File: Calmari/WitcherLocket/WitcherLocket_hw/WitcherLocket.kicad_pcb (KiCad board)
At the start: 2 copper layers, 41 x 50 mm, 31 parts, among them SW1 SWITCH_2X, SW2 SWITCH_2X, SW3 SWITCH_2X, SW4 SWITCH_2X

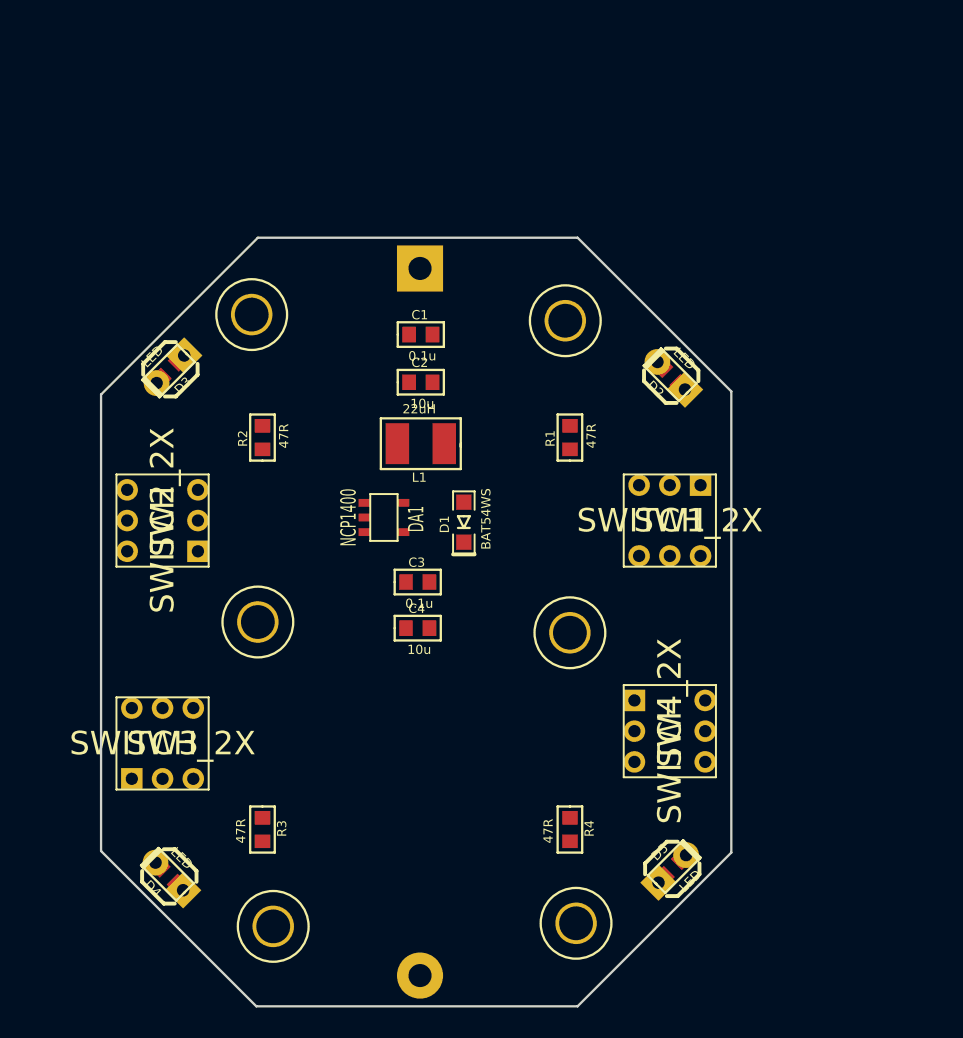
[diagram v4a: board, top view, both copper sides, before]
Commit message: 
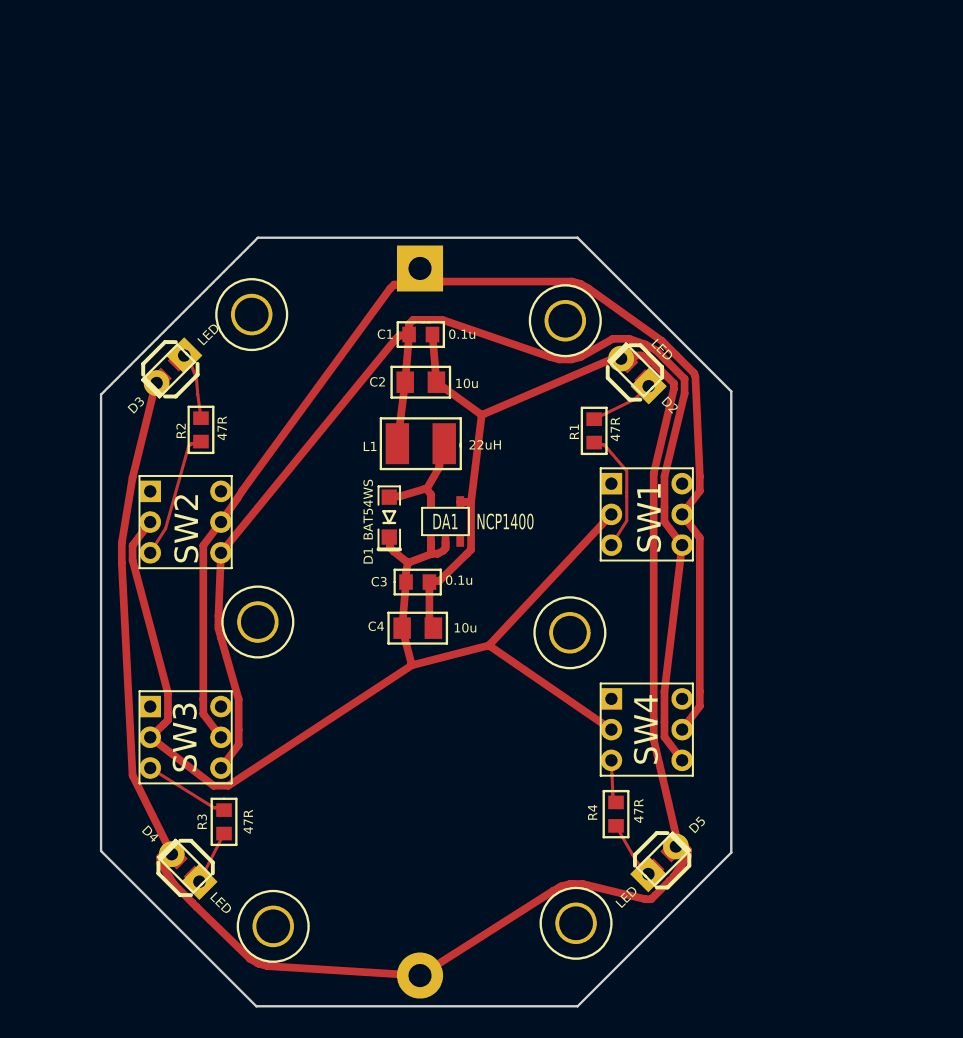
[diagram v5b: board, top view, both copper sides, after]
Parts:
- C2, C4: footprint CAP_0603 -> CAP_0805
- moved D1 4.86 mm to (153.2, 117.2)
- moved R2 4.03 mm to (141.0, 111.5)
- moved DA1 4.02 mm to (156.9, 117.5), turned to 0 degrees
- moved R4 3.16 mm to (168.0, 136.5)
- moved R3 2.55 mm to (142.5, 137.0)
- moved D6 2.37 mm to (169.2, 107.8)
- moved D2 2.30 mm to (169.3, 107.7)
- moved R1 1.64 mm to (166.6, 111.6)
- moved SW1 1.55 mm to (170.0, 117.0), turned to 270 degrees
- moved SW3 1.55 mm to (140.0, 131.5), turned to 270 degrees
- moved SW2 1.50 mm to (140.0, 117.5), turned to 270 degrees
- moved SW4 1.50 mm to (170.0, 131.0)
- moved D4 1.23 mm to (140.0, 140.0)
- moved D8 1.19 mm to (140.0, 140.0)
- moved D9 0.87 mm to (171.0, 139.5)
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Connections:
- SW1 pad 4: (no net) -> /PWR_IN
- SW1 pad 6: /PWR_IN -> (no net)
- SW2 pad 4: (no net) -> /PWR_IN
- SW2 pad 6: /PWR_IN -> (no net)
- SW3 pad 4: (no net) -> /PWR_IN
- SW3 pad 6: /PWR_IN -> (no net)
- SW4 pad 4: (no net) -> /PWR_IN
- SW4 pad 6: /PWR_IN -> (no net)
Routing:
- net GND: track 0.00 -> 143.4 mm
- net /PWR_IN: track 0.00 -> 86.9 mm
- net +BATT: track 0.00 -> 80.5 mm
- net +3.3V: track 0.00 -> 75.1 mm
- net N-000002: track 0.00 -> 8.32 mm
- net N-0000011: track 0.00 -> 8.03 mm
- net /Lout: track 0.00 -> 6.66 mm
- net N-000007: track 0.00 -> 5.57 mm
- net N-0000024: track 0.00 -> 5.11 mm
- net N-0000022: track 0.00 -> 4.69 mm
- net N-0000013: track 0.00 -> 4.31 mm
- net N-0000012: track 0.00 -> 4.04 mm
- net N-0000010: track 0.00 -> 2.80 mm
- added copper zone on F.Cu, net GND
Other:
- rule pad_to_mask_clearance: 0 -> 0.1

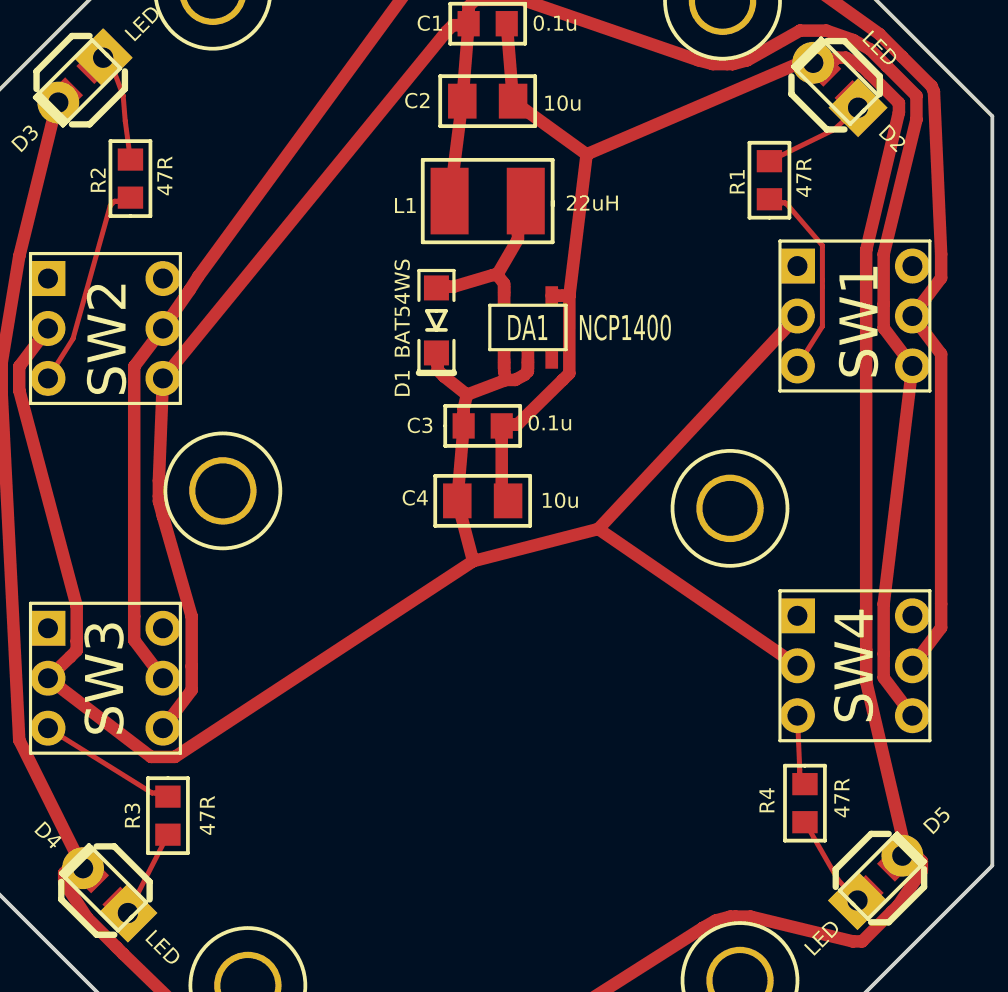
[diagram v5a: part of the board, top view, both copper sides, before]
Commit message: led resistors change
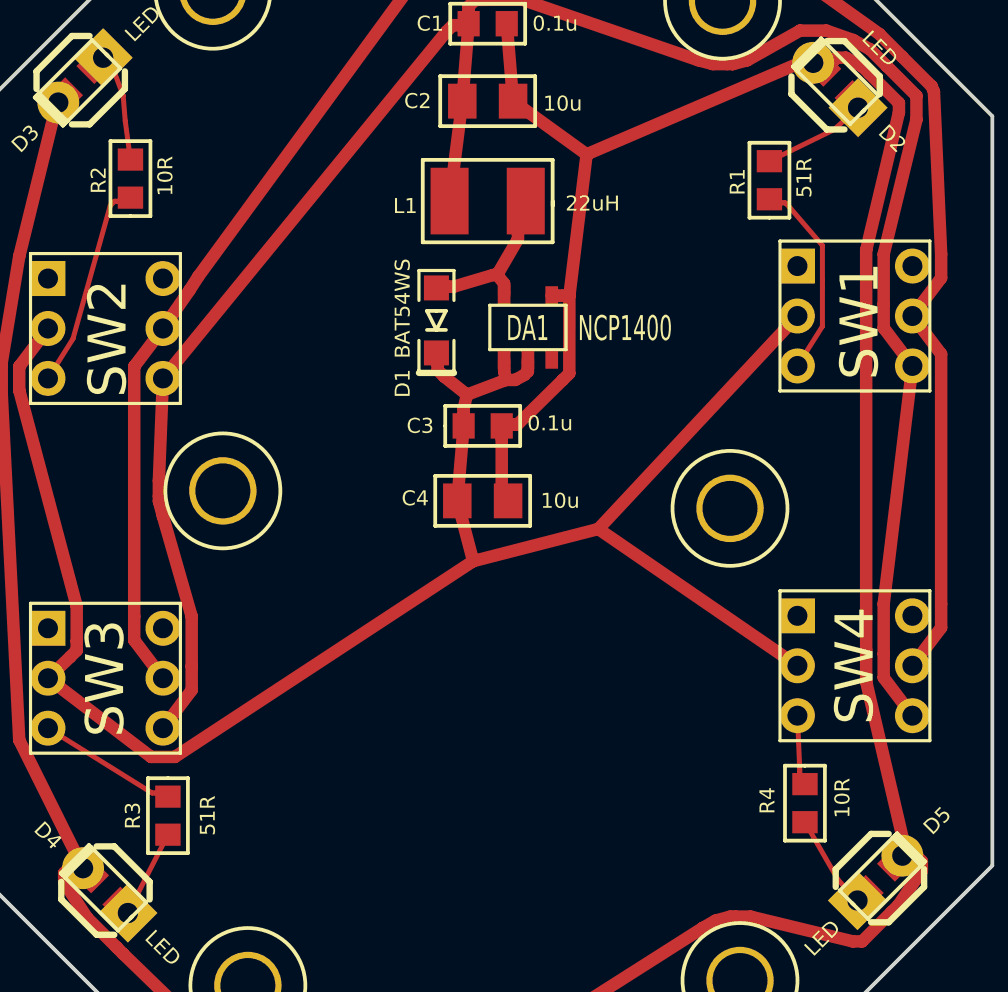
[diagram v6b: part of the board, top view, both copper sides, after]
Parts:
- R1, R3: value 47R -> 51R
- R2, R4: value 47R -> 10R
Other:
- board text added: "Blue"
- board text added: "Green"
- board text added: "Red"
- board text added: "Yellow"
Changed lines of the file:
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@@
-(kicad_pcb (version 3) (host pcbnew "(2013-03-19 BZR 4004)-stable")
+(kicad_pcb (version 3) (host pcbnew "(2013-05-16 BZR 4016)-stable")
   (general
     (links 45)
@@
     (area 133.4736 98.624863 175.9264 149.100001)
     (thickness 1.6)
-    (drawings 13)
+    (drawings 17)
     (tracks 238)
     (zones 0)
@@
       (usegerberextensions true)
       (excludeedgelayer true)
-      (linewidth 152400)
+      (linewidth 0.150000)
       (plotframeref false)
       (viasonmask false)
@@
       (effects (font (size 0.6 0.6) (thickness 0.15)))
     )
-    (fp_text value 47R (at 0 -1.6 270) (layer F.SilkS)
+    (fp_text value 51R (at 0 -1.6 270) (layer F.SilkS)
       (effects (font (size 0.6 0.6) (thickness 0.15)))
     )
@@
       (effects (font (size 0.6 0.6) (thickness 0.15)))
     )
-    (fp_text value 47R (at -0.2 -1.5 270) (layer F.SilkS)
+    (fp_text value 10R (at -0.2 -1.5 270) (layer F.SilkS)
       (effects (font (size 0.6 0.6) (thickness 0.15)))
     )
@@
       (effects (font (size 0.6 0.6) (thickness 0.15)))
     )
-    (fp_text value 47R (at 0.09906 1.39954 90) (layer F.SilkS)
+    (fp_text value 10R (at 0.09906 1.39954 90) (layer F.SilkS)
       (effects (font (size 0.6 0.6) (thickness 0.15)))
     )
@@
       (effects (font (size 0.6 0.6) (thickness 0.15)))
     )
-    (fp_text value 47R (at 0.09906 1.39954 90) (layer F.SilkS)
+    (fp_text value 51R (at 0.09906 1.39954 90) (layer F.SilkS)
       (effects (font (size 0.6 0.6) (thickness 0.15)))
     )
@@
     )
   )
+  (gr_text Green (at 166 139.5) (layer Cmts.User)
+    (effects (font (size 1 1) (thickness 0.25)))
+  )
+  (gr_text Red (at 144 140) (layer Cmts.User)
+    (effects (font (size 1 1) (thickness 0.25)))
+  )
+  (gr_text Yellow (at 165.5 109) (layer Cmts.User)
+    (effects (font (size 1 1) (thickness 0.25)))
+  )
+  (gr_text Blue (at 143 108.5) (layer Cmts.User)
+    (effects (font (size 1 1) (thickness 0.25)))
+  )
   (gr_line (start 134.5 109.2) (end 144.7 99) (angle 90) (layer Edge.Cuts) (width 0.15))
